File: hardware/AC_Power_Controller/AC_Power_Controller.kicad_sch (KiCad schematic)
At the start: 20 parts, among them J1 230VAC_IN, U1 MOC3023M, U2 ADS1115IDGS, U3 ZMPT101B, U4 PC814, U5 SCT_013_030

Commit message: corrections to schematics
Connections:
- net at R7.1, U3.4 (OUT): now also A1.9 (A0); no longer A1.30 (AREF)
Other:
- title: (none) -> AC_Power_Controller
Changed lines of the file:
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@@
 	(paper "A4")
 	(title_block
-		(date "2025-10-31")
-		(rev "1.0")
+		(title "AC_Power_Controller")
+		(date "2025-11-01")
+		(rev "1.1")
 	)
 	(junction
@@
 	(wire
 		(pts
-			(xy 146.05 157.48) (xy 76.2 157.48)
-		)
-		(stroke
-			(width 0)
-			(type default)
-		)
-	)
-	(wire
-		(pts
 			(xy 151.13 111.76) (xy 86.36 111.76)
 		)
@@
 	(wire
 		(pts
-			(xy 146.05 142.24) (xy 146.05 157.48)
-		)
-		(stroke
-			(width 0)
-			(type default)
-		)
-	)
-	(wire
-		(pts
 			(xy 64.77 99.06) (xy 64.77 107.95)
 		)
@@
 	(wire
 		(pts
+			(xy 140.97 142.24) (xy 140.97 157.48)
+		)
+		(stroke
+			(width 0)
+			(type default)
+		)
+	)
+	(wire
+		(pts
 			(xy 236.22 58.42) (xy 245.11 58.42)
 		)
@@
 		)
 		(stroke
+			(width 0)
+			(type default)
+		)
+	)
+	(wire
+		(pts
+			(xy 140.97 157.48) (xy 76.2 157.48)
+		)
+		(stroke

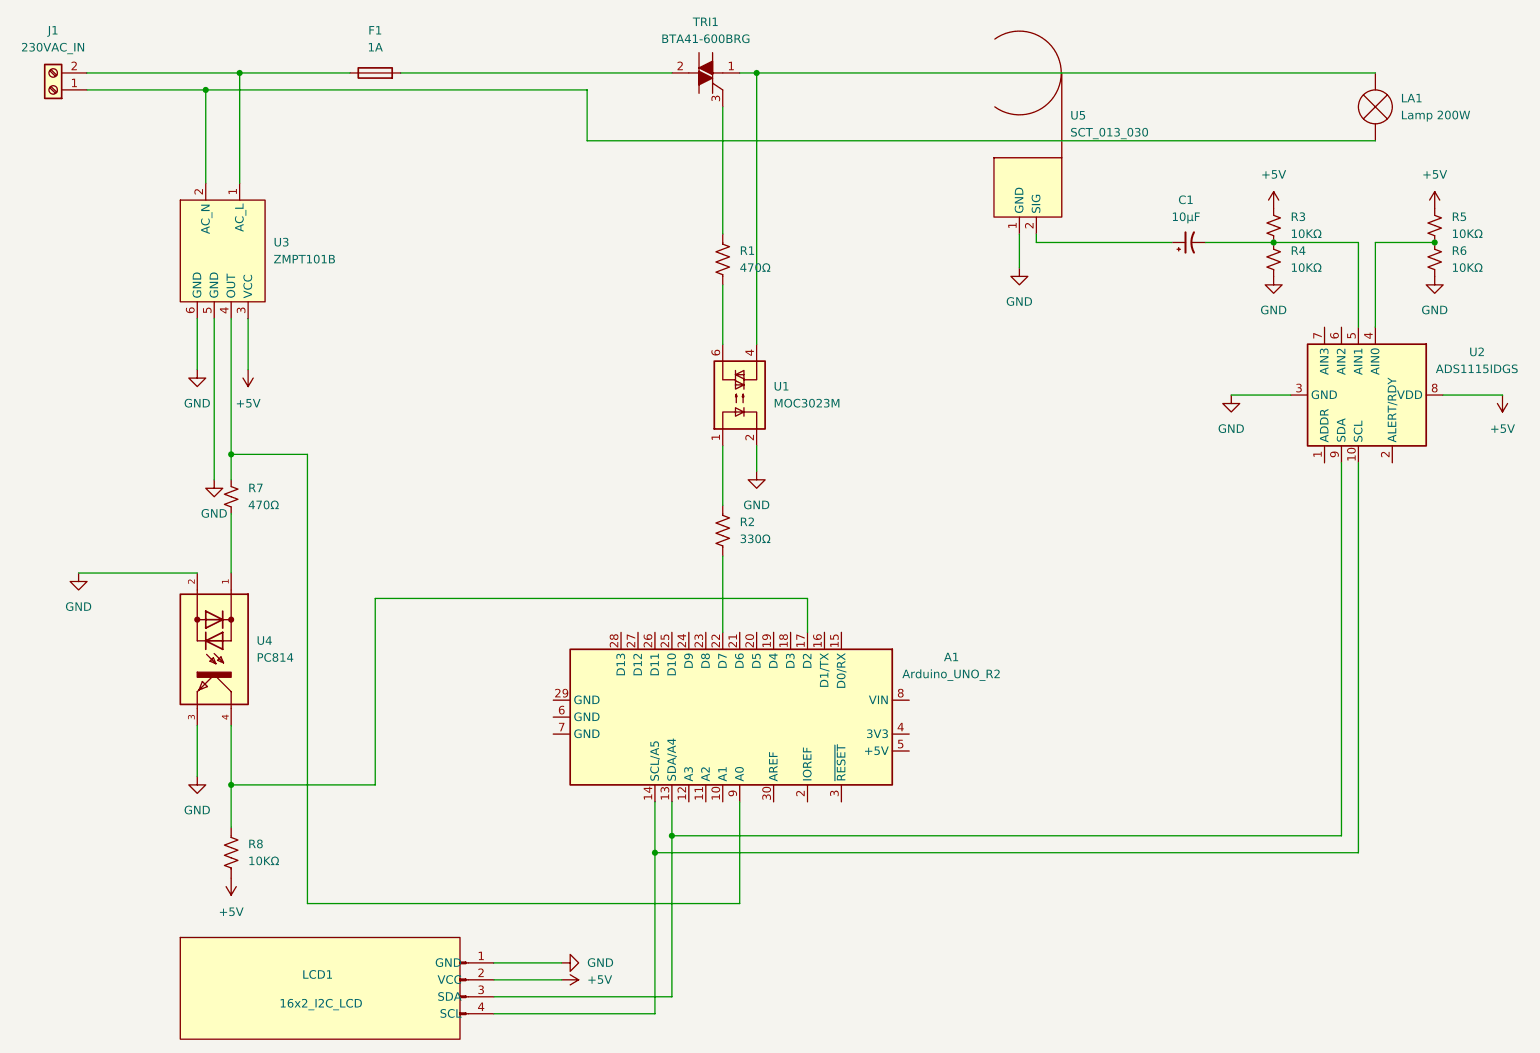
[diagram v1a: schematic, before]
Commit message: schematic corrections
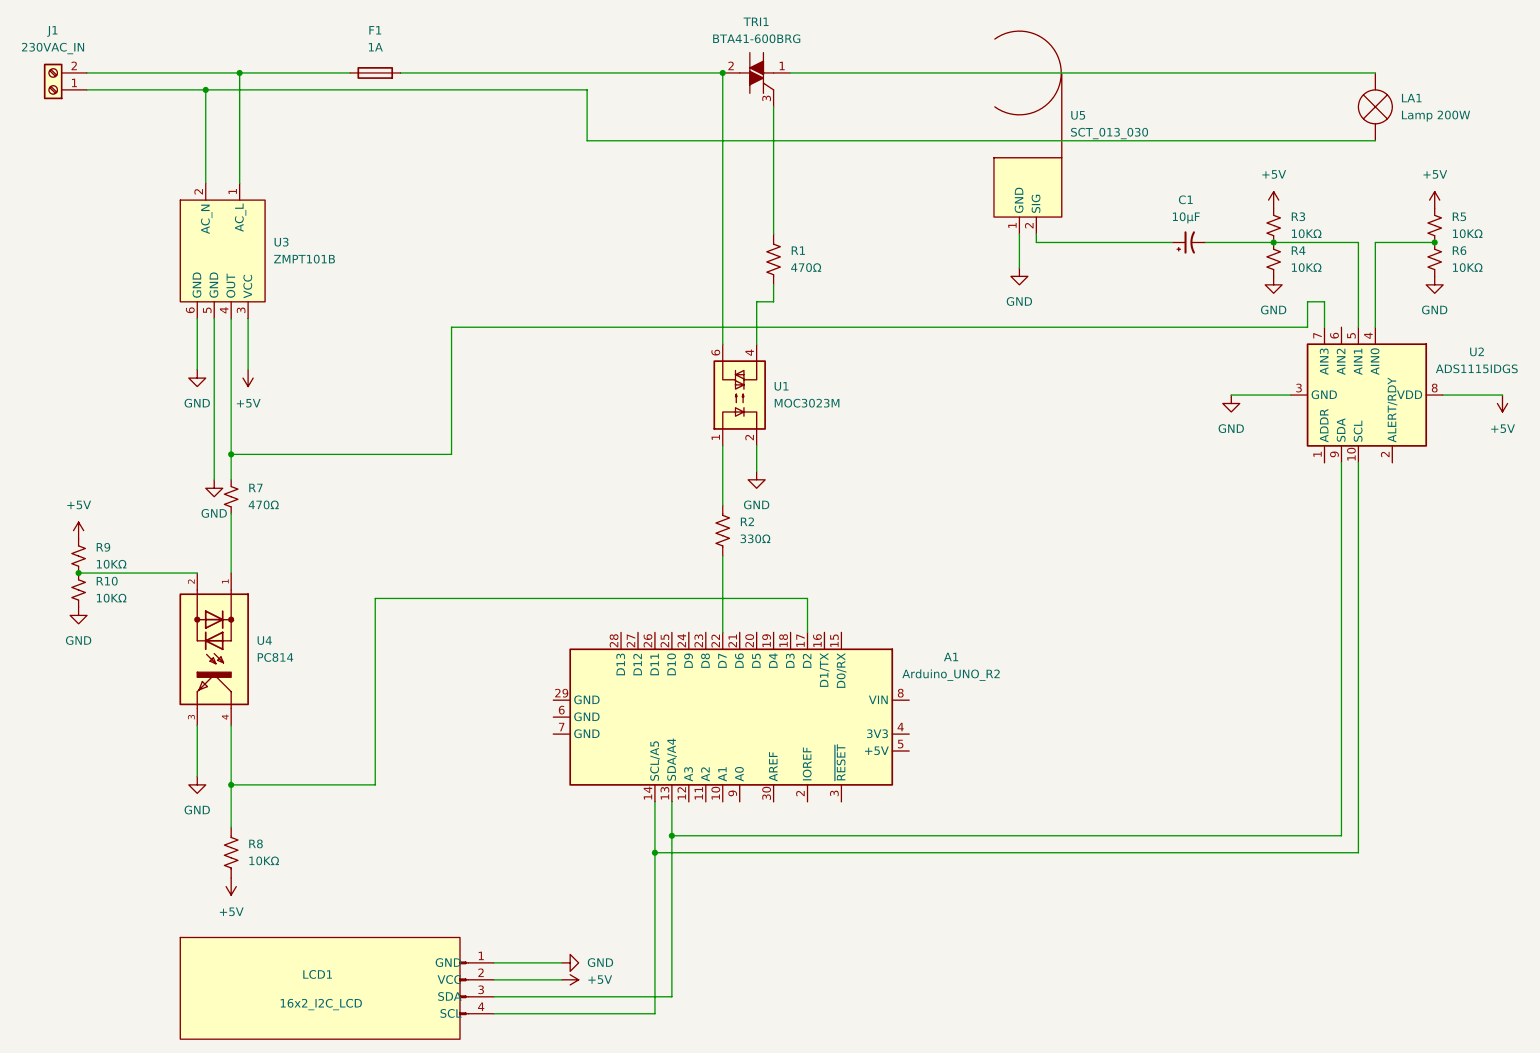
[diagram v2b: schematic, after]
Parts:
- added R10: 10KΩ, symbol Device:R_Small_US
- added R9: 10KΩ, Resistor_THT:R_Axial_DIN0204_L3.6mm_D1.6mm_P1.90mm_Vertical, symbol Device:R_Small_US
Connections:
- net +5V: now also R9.1
- net GND: now also R10.2; no longer U4.2
- net at R7.1, U3.4 (OUT): now also U2.7 (AIN3); no longer A1.9 (A0)
- net at LA1.2 (+), TRI1.1 (A1): no longer U1.4
- net at F1.2, TRI1.2 (A2): now also U1.6
- net at R1.2: now also U1.4; no longer U1.6
- new net: R10.1, R9.2, U4.2
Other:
- moved on the sheet: R1, TRI1

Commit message: update
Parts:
- removed R10: 10KΩ, symbol Device:R_Small_US
- removed R7: 470Ω, Resistor_THT:R_Axial_DIN0204_L3.6mm_D1.6mm_P5.08mm_Horizontal, symbol Device:R_Small_US
- removed R9: 10KΩ, Resistor_THT:R_Axial_DIN0204_L3.6mm_D1.6mm_P1.90mm_Vertical, symbol Device:R_Small_US
- added T1: Transformer_230V_12V, symbol Device:Transformer_1P_SS
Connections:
- net at F1.1, J1.2 (Pin_2): now also T1.1 (AA); no longer U3.1 (AC_L)
- net at J1.1 (Pin_1), LA1.1 (-), U3.2 (AC_N): now also T1.2 (AB)
- net at LA1.2 (+), TRI1.1 (A1): now also U3.1 (AC_L)
- net at U4.1: now also T1.5 (SB)
- net at U4.2: now also T1.4 (SC)
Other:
- moved on the sheet: U3, U5
